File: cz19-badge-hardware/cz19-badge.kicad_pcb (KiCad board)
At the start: 4 copper layers, 169 x 56.5 mm, 445 parts, among them J1 USB_B_Micro, Q1 AO3400 (A09T), Q2 AO3400 (A09T), Q3 AO3400 (A09T), Q4 AO3400 (A09T), Q5 AO3400 (A09T), Q6 AO3400 (A09T), Q7 AO3400 (A09T), Q8 AO3400 (A09T), Q9 AO3400 (A09T), SW1 SW_Push, SW2 SW_Push, SW3 SW_Push, SW4 SW_Push, SW5 SW_Push, SW6 SW_Push, U1 CH340C, U2 AMS1117, U3 ESP32-WROOM-32D, U4 TP4056

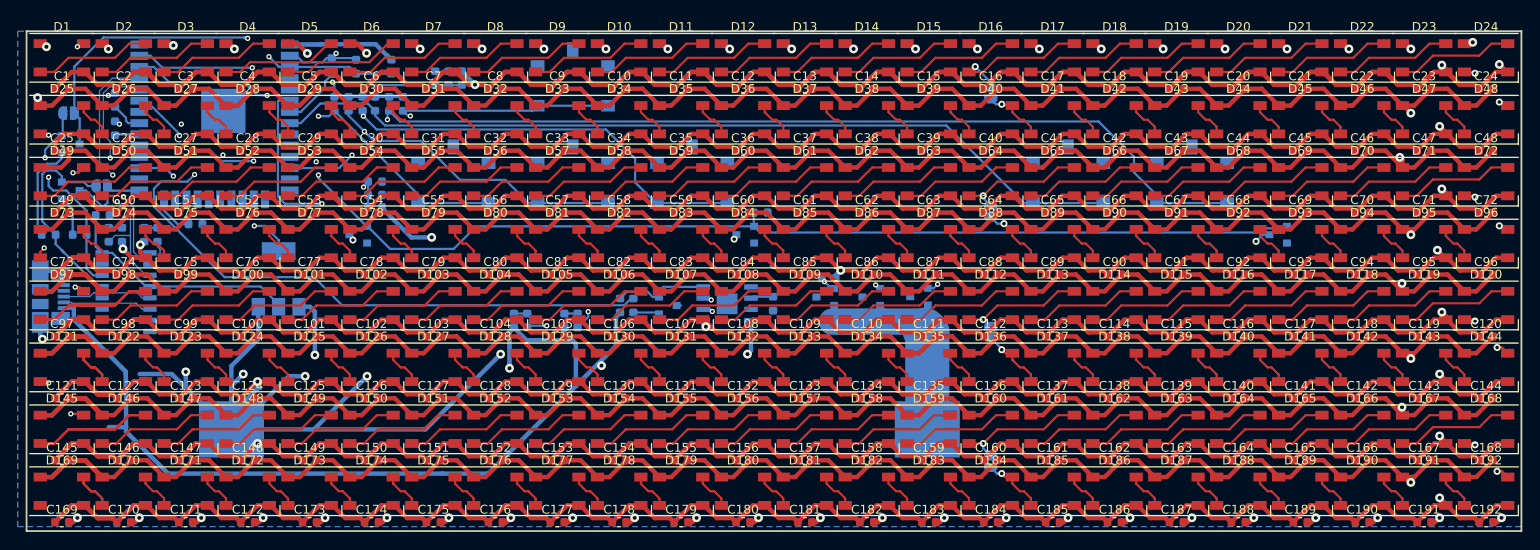
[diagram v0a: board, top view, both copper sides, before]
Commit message: Added experimental touch pad to center
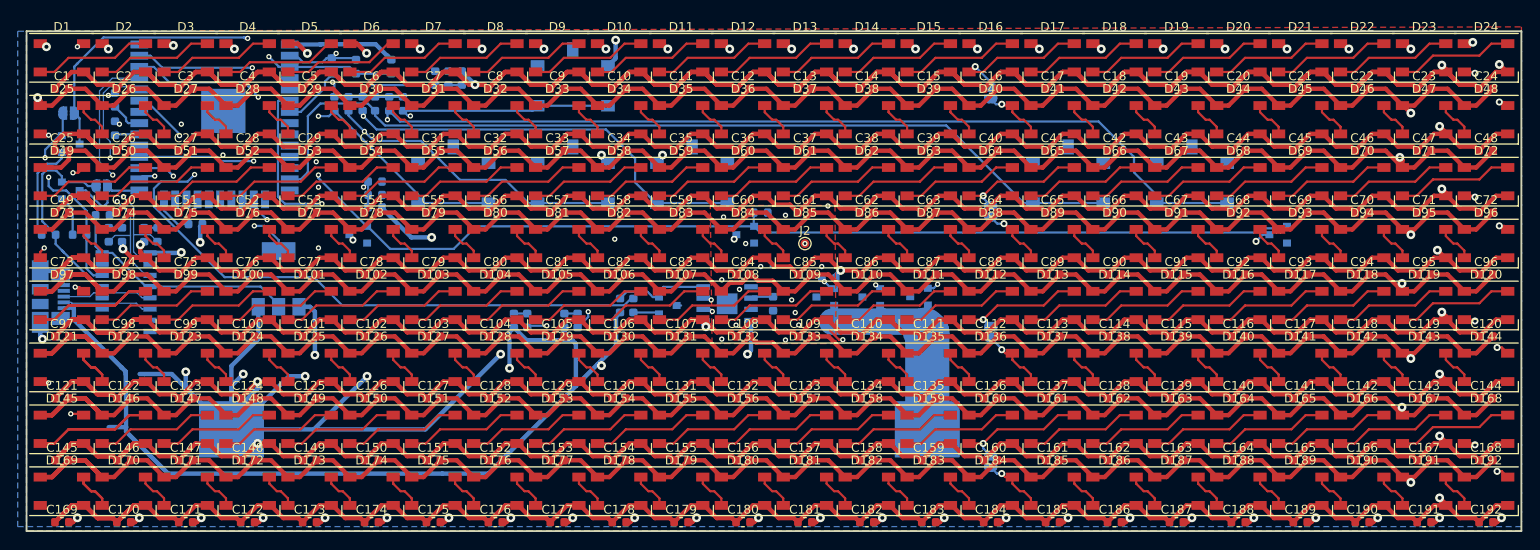
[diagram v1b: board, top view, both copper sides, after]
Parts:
- added J2: Conn_01x01, TestPoint:TestPoint_Pad_D1.0mm, F.Cu at (108.0, 46.0)
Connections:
- U1 pad 1: (no net) -> GND
- U3 pad 12: BTN_A -> (no net)
- U3 pad 13: (no net) -> BTN_B
- U3 pad 16: (no net) -> BTN_A
- U3 pad 26: (no net) -> TOUCH1
- U3 pad 8: BTN_B -> (no net)
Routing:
- net TOUCH1: track 0.00 -> 140.2 mm, vias 0 -> 19
- net GND: track 57.0 -> 92.1 mm, vias 2 -> 7
- net BTN_A: track 115.0 -> 122.9 mm, vias 2 -> 3
- net BTN_B: track 97.9 -> 104.2 mm
- added copper zone on F.Cu, net LED_GND
- added copper zone on F.Cu, net TOUCH1

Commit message: Fixed DRC warning
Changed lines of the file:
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@@
     (thickness 1.6)
     (drawings 8)
-    (tracks 3638)
+    (tracks 3639)
     (zones 0)
     (modules 446)
@@
   (segment (start 44.6 27.759998) (end 36.124998 27.759998) (width 0.25) (layer GND.Cu) (net 228))
   (segment (start 32.75 26.035) (end 34.4 26.035) (width 0.25) (layer GND.Cu) (net 228))
-  (via (at 46.20107 29.448029) (size 0.6) (drill 0.3) (layers F.Cu GND.Cu) (net 228))
-  (segment (start 45.840002 29) (end 45.840002 29.086961) (width 0.25) (layer GND.Cu) (net 228))
-  (segment (start 45.840002 29.086961) (end 46.20107 29.448029) (width 0.25) (layer GND.Cu) (net 228))
   (segment (start 44.6 27.759998) (end 45.840002 29) (width 0.25) (layer GND.Cu) (net 228))
-  (segment (start 51.3 29.9) (end 53 31.6) (width 0.25) (layer LGND.Cu) (net 228))
-  (segment (start 50.848029 29.448029) (end 51.3 29.9) (width 0.25) (layer LGND.Cu) (net 228))
-  (segment (start 46.20107 29.448029) (end 50.848029 29.448029) (width 0.25) (layer LGND.Cu) (net 228))
+  (via (at 46.2 29.8) (size 0.6) (drill 0.3) (layers F.Cu GND.Cu) (net 228))
+  (segment (start 53 31.6) (end 51.2 29.8) (width 0.25) (layer LGND.Cu) (net 228))
+  (segment (start 51.2 29.8) (end 46.624264 29.8) (width 0.25) (layer LGND.Cu) (net 228))
+  (segment (start 46.624264 29.8) (end 46.2 29.8) (width 0.25) (layer LGND.Cu) (net 228))
+  (segment (start 45.840002 29.015738) (end 45.840002 29) (width 0.25) (layer GND.Cu) (net 228))
+  (segment (start 46.2 29.375736) (end 45.840002 29.015738) (width 0.25) (layer GND.Cu) (net 228))
+  (segment (start 46.2 29.8) (end 46.2 29.375736) (width 0.25) (layer GND.Cu) (net 228))
   (segment (start 91.145 41.42) (end 91.27 41.42) (width 0.25) (layer GND.Cu) (net 229))
   (segment (start 88.8 39.075) (end 91.145 41.42) (width 0.25) (layer GND.Cu) (net 229))
@@
     (connect_pads (clearance 0.508))
     (min_thickness 0.254)
-    (fill yes (arc_segments 16) (thermal_gap 0.508) (thermal_bridge_width 0.508))
+    (fill yes (arc_segments 16) (thermal_gap 0.508) (thermal_bridge_width 0.3))
     (polygon
       (pts

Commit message: Added testpoint hooks
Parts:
- added J3: Hook1, TestPoint:TestPoint_Keystone_5019_Minature, B.Cu at (27.2, 26.2)
- added J4: Hook2, TestPoint:TestPoint_Keystone_5019_Minature, B.Cu at (173.6, 26.2)
- added J5: Hook3, TestPoint:TestPoint_Keystone_5019_Minature, B.Cu at (143.3, 63.7)
- added J6: Hook4, TestPoint:TestPoint_Keystone_5019_Minature, B.Cu at (158.3, 63.7)
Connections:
- D169 pad 4: (no net) -> LEDS_OUT
- J1 pad 4: (no net) -> Net-(J1-Pad4)
- U1 pad 10: (no net) -> Net-(U1-Pad10)
- U1 pad 11: (no net) -> Net-(U1-Pad11)
- U1 pad 12: (no net) -> Net-(U1-Pad12)
- U1 pad 15: (no net) -> Net-(U1-Pad15)
- U1 pad 7: (no net) -> Net-(U1-Pad7)
- U1 pad 8: (no net) -> Net-(U1-Pad8)
- U1 pad 9: (no net) -> Net-(U1-Pad9)
- U3 pad 10: (no net) -> DAC1
- U3 pad 11: (no net) -> DAC2
- U3 pad 12: (no net) -> Net-(U3-Pad12)
- U3 pad 14: (no net) -> Net-(U3-Pad14)
- U3 pad 17: (no net) -> Net-(U3-Pad17)
- U3 pad 18: (no net) -> Net-(U3-Pad18)
- U3 pad 19: (no net) -> Net-(U3-Pad19)
- U3 pad 20: (no net) -> Net-(U3-Pad20)
- U3 pad 21: (no net) -> Net-(U3-Pad21)
- U3 pad 22: (no net) -> Net-(U3-Pad22)
- U3 pad 23: (no net) -> Net-(U3-Pad23)
- U3 pad 29: (no net) -> Net-(U3-Pad29)
- U3 pad 32: (no net) -> Net-(U3-Pad32)
- U3 pad 4: (no net) -> Net-(U3-Pad4)
- U3 pad 5: (no net) -> Net-(U3-Pad5)
- U3 pad 8: (no net) -> Net-(U3-Pad8)
- U3 pad 9: (no net) -> Net-(U3-Pad9)
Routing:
- net ESP_EN: track 48.7 -> 51.4 mm
- net LEDS_IN: track 8.66 -> 9.71 mm
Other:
- board text added: "CZ19 1337 badge proto v0.1 aka “Harry Potter”"
- board text added: "Spoke width: 0.508mm"
- board text added: "Spoke width: 0.8mm"
- board text added: "Spoke width: 1.2mm"

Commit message: Working on non-smart leds
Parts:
- removed the C1 at (24.0, 28.5)
- removed C10, C100, C101, C102, C103, C104, C105, C106, C107, C108, C109, C11, C110, C111, C112, C113, C114, C115, C116, C117, C118, C119, C12, C120, C121, C122, C123, C124, C125, C126, C127, C128, C129, C13, C130, C131, C132, C133, C134, C135, C136, C137, C138, C139, C14, C140, C141, C142, C143, C144, C145, C146, C147, C148, C149, C15, C150, C151, C152, C153, C154, C155, C156, C157, C158, C159, C16, C160, C161, C162, C163, C164, C165, C166, C167, C168, C169, C17, C170, C171, C172, C173, C174, C175, C176, C177, C178, C179, C18, C180, C181, C182, C183, C184, C185, C186, C187, C188, C189, C19, C190, C191, C192, C20, C21, C22, C23, C24, C25, C26, C27, C28, C29, C30, C31, C32, C33, C34, C35, C36, C37, C38, C39, C40, C41, C42, C43, C44, C45, C46, C47, C48, C49, C5, C50, C51, C52, C53, C54, C55, C56, C57, C58, C59, C6, C60, C61, C62, C63, C64, C65, C66, C67, C68, C69, C7, C70, C71, C72, C73, C74, C75, C76, C77, C78, C79, C8, C80, C81, C82, C83, C84, C85, C86, C87, C88, C89, C9, C90, C91, C92, C93, C94, C95, C96, C97, C98, C99: 100nF, Capacitor_SMD:C_0603_1608Metric
- removed the C2 at (31.0, 28.5)
- removed the C3 at (38.0, 28.5)
- removed the C4 at (45.0, 28.5)
- removed J2: Conn_01x01, TestPoint:TestPoint_Pad_D1.0mm
- removed J5: Hook3, TestPoint:TestPoint_Keystone_5019_Minature
- removed J6: Hook4, TestPoint:TestPoint_Keystone_5019_Minature
- removed JP1, JP2, JP3, JP4, JP5, JP6: SolderJumper_2_Open, Jumper:SolderJumper-2_P1.3mm_Open_RoundedPad1.0x1.5mm
- removed the Q1 at (57.5, 45.0)
- removed the Q3 at (101.2, 45.0)
- removed the Q5 at (161.5, 45.0)
- removed the R8 at (30.0, 33.0)
- removed the R9 at (30.0, 29.8)
- added D193: LED_RGBA, LED_SMD:LED_Cree-PLCC4_3.2x2.8mm_CCW, F.Cu at (20.0, -120.0)
- added D194: LED_RGBA, LED_SMD:LED_Cree-PLCC4_3.2x2.8mm_CCW, F.Cu at (25.0, -120.0)
- added D195: LED_RGBA, LED_SMD:LED_Cree-PLCC4_3.2x2.8mm_CCW, F.Cu at (30.0, -120.0)
- added D196: LED_RGBA, LED_SMD:LED_Cree-PLCC4_3.2x2.8mm_CCW, F.Cu at (35.0, -120.0)
- added D197: LED_RGBA, LED_SMD:LED_Cree-PLCC4_3.2x2.8mm_CCW, F.Cu at (40.0, -120.0)
- added D198: LED_RGBA, LED_SMD:LED_Cree-PLCC4_3.2x2.8mm_CCW, F.Cu at (45.0, -120.0)
- added D199: LED_RGBA, LED_SMD:LED_Cree-PLCC4_3.2x2.8mm_CCW, F.Cu at (50.0, -120.0)
- added D200: LED_RGBA, LED_SMD:LED_Cree-PLCC4_3.2x2.8mm_CCW, F.Cu at (55.0, -120.0)
- added D201: LED_RGBA, LED_SMD:LED_Cree-PLCC4_3.2x2.8mm_CCW, F.Cu at (60.0, -120.0)
- added D202: LED_RGBA, LED_SMD:LED_Cree-PLCC4_3.2x2.8mm_CCW, F.Cu at (65.0, -120.0)
- added D203: LED_RGBA, LED_SMD:LED_Cree-PLCC4_3.2x2.8mm_CCW, F.Cu at (70.0, -120.0)
- added D204: LED_RGBA, LED_SMD:LED_Cree-PLCC4_3.2x2.8mm_CCW, F.Cu at (75.0, -120.0)
- added D205: LED_RGBA, LED_SMD:LED_Cree-PLCC4_3.2x2.8mm_CCW, F.Cu at (80.0, -120.0)
- added D206: LED_RGBA, LED_SMD:LED_Cree-PLCC4_3.2x2.8mm_CCW, F.Cu at (85.0, -120.0)
- added D207: LED_RGBA, LED_SMD:LED_Cree-PLCC4_3.2x2.8mm_CCW, F.Cu at (90.0, -120.0)
- added D208: LED_RGBA, LED_SMD:LED_Cree-PLCC4_3.2x2.8mm_CCW, F.Cu at (95.0, -120.0)
- added D209: LED_RGBA, LED_SMD:LED_Cree-PLCC4_3.2x2.8mm_CCW, F.Cu at (100.0, -120.0)
- added D210: LED_RGBA, LED_SMD:LED_Cree-PLCC4_3.2x2.8mm_CCW, F.Cu at (105.0, -120.0)
- added D211: LED_RGBA, LED_SMD:LED_Cree-PLCC4_3.2x2.8mm_CCW, F.Cu at (110.0, -120.0)
- added D212: LED_RGBA, LED_SMD:LED_Cree-PLCC4_3.2x2.8mm_CCW, F.Cu at (115.0, -120.0)
- added D213: LED_RGBA, LED_SMD:LED_Cree-PLCC4_3.2x2.8mm_CCW, F.Cu at (120.0, -120.0)
- added D214: LED_RGBA, LED_SMD:LED_Cree-PLCC4_3.2x2.8mm_CCW, F.Cu at (125.0, -120.0)
- added D215: LED_RGBA, LED_SMD:LED_Cree-PLCC4_3.2x2.8mm_CCW, F.Cu at (130.0, -120.0)
- added D216: LED_RGBA, LED_SMD:LED_Cree-PLCC4_3.2x2.8mm_CCW, F.Cu at (135.0, -120.0)
- added D217: LED_RGBA, LED_SMD:LED_Cree-PLCC4_3.2x2.8mm_CCW, F.Cu at (140.0, -120.0)
- added D218: LED_RGBA, LED_SMD:LED_Cree-PLCC4_3.2x2.8mm_CCW, F.Cu at (145.0, -120.0)
- added D219: LED_RGBA, LED_SMD:LED_Cree-PLCC4_3.2x2.8mm_CCW, F.Cu at (150.0, -120.0)
- added D220: LED_RGBA, LED_SMD:LED_Cree-PLCC4_3.2x2.8mm_CCW, F.Cu at (155.0, -120.0)
- added D221: LED_RGBA, LED_SMD:LED_Cree-PLCC4_3.2x2.8mm_CCW, F.Cu at (160.0, -120.0)
- added D222: LED_RGBA, LED_SMD:LED_Cree-PLCC4_3.2x2.8mm_CCW, F.Cu at (165.0, -120.0)
- added D223: LED_RGBA, LED_SMD:LED_Cree-PLCC4_3.2x2.8mm_CCW, F.Cu at (170.0, -120.0)
- added D224: LED_RGBA, LED_SMD:LED_Cree-PLCC4_3.2x2.8mm_CCW, F.Cu at (175.0, -120.0)
- added D225: LED_RGBA, LED_SMD:LED_Cree-PLCC4_3.2x2.8mm_CCW, F.Cu at (20.0, -115.0)
- added D226: LED_RGBA, LED_SMD:LED_Cree-PLCC4_3.2x2.8mm_CCW, F.Cu at (25.0, -115.0)
- added D227: LED_RGBA, LED_SMD:LED_Cree-PLCC4_3.2x2.8mm_CCW, F.Cu at (30.0, -115.0)
- added D228: LED_RGBA, LED_SMD:LED_Cree-PLCC4_3.2x2.8mm_CCW, F.Cu at (35.0, -115.0)
- added D229: LED_RGBA, LED_SMD:LED_Cree-PLCC4_3.2x2.8mm_CCW, F.Cu at (40.0, -115.0)
- added D230: LED_RGBA, LED_SMD:LED_Cree-PLCC4_3.2x2.8mm_CCW, F.Cu at (45.0, -115.0)
- added D231: LED_RGBA, LED_SMD:LED_Cree-PLCC4_3.2x2.8mm_CCW, F.Cu at (50.0, -115.0)
- added D232: LED_RGBA, LED_SMD:LED_Cree-PLCC4_3.2x2.8mm_CCW, F.Cu at (55.0, -115.0)
- added D233: LED_RGBA, LED_SMD:LED_Cree-PLCC4_3.2x2.8mm_CCW, F.Cu at (60.0, -115.0)
- added D234: LED_RGBA, LED_SMD:LED_Cree-PLCC4_3.2x2.8mm_CCW, F.Cu at (65.0, -115.0)
- added D235: LED_RGBA, LED_SMD:LED_Cree-PLCC4_3.2x2.8mm_CCW, F.Cu at (70.0, -115.0)
- added D236: LED_RGBA, LED_SMD:LED_Cree-PLCC4_3.2x2.8mm_CCW, F.Cu at (75.0, -115.0)
- added D237: LED_RGBA, LED_SMD:LED_Cree-PLCC4_3.2x2.8mm_CCW, F.Cu at (80.0, -115.0)
- added D238: LED_RGBA, LED_SMD:LED_Cree-PLCC4_3.2x2.8mm_CCW, F.Cu at (85.0, -115.0)
- added D239: LED_RGBA, LED_SMD:LED_Cree-PLCC4_3.2x2.8mm_CCW, F.Cu at (90.0, -115.0)
- added D240: LED_RGBA, LED_SMD:LED_Cree-PLCC4_3.2x2.8mm_CCW, F.Cu at (95.0, -115.0)
- added D241: LED_RGBA, LED_SMD:LED_Cree-PLCC4_3.2x2.8mm_CCW, F.Cu at (100.0, -115.0)
- added D242: LED_RGBA, LED_SMD:LED_Cree-PLCC4_3.2x2.8mm_CCW, F.Cu at (105.0, -115.0)
- added D243: LED_RGBA, LED_SMD:LED_Cree-PLCC4_3.2x2.8mm_CCW, F.Cu at (110.0, -115.0)
- added D244: LED_RGBA, LED_SMD:LED_Cree-PLCC4_3.2x2.8mm_CCW, F.Cu at (115.0, -115.0)
- added D245: LED_RGBA, LED_SMD:LED_Cree-PLCC4_3.2x2.8mm_CCW, F.Cu at (120.0, -115.0)
- added D246: LED_RGBA, LED_SMD:LED_Cree-PLCC4_3.2x2.8mm_CCW, F.Cu at (125.0, -115.0)
- added D247: LED_RGBA, LED_SMD:LED_Cree-PLCC4_3.2x2.8mm_CCW, F.Cu at (130.0, -115.0)
- added D248: LED_RGBA, LED_SMD:LED_Cree-PLCC4_3.2x2.8mm_CCW, F.Cu at (135.0, -115.0)
- added D249: LED_RGBA, LED_SMD:LED_Cree-PLCC4_3.2x2.8mm_CCW, F.Cu at (140.0, -115.0)
- added D250: LED_RGBA, LED_SMD:LED_Cree-PLCC4_3.2x2.8mm_CCW, F.Cu at (145.0, -115.0)
- added D251: LED_RGBA, LED_SMD:LED_Cree-PLCC4_3.2x2.8mm_CCW, F.Cu at (150.0, -115.0)
- added D252: LED_RGBA, LED_SMD:LED_Cree-PLCC4_3.2x2.8mm_CCW, F.Cu at (155.0, -115.0)
- added D253: LED_RGBA, LED_SMD:LED_Cree-PLCC4_3.2x2.8mm_CCW, F.Cu at (160.0, -115.0)
- added D254: LED_RGBA, LED_SMD:LED_Cree-PLCC4_3.2x2.8mm_CCW, F.Cu at (165.0, -115.0)
- added D255: LED_RGBA, LED_SMD:LED_Cree-PLCC4_3.2x2.8mm_CCW, F.Cu at (170.0, -115.0)
- added D256: LED_RGBA, LED_SMD:LED_Cree-PLCC4_3.2x2.8mm_CCW, F.Cu at (175.0, -115.0)
- added R1: R, Resistor_SMD:R_0603_1608Metric, F.Cu at (263.2, 108.0)
- added R20: 10k, Resistor_SMD:R_0603_1608Metric, F.Cu at (239.2, 116.3)
- added R21: 10k, Resistor_SMD:R_0603_1608Metric, F.Cu at (239.2, 114.8)
- added R23: 10k, Resistor_SMD:R_0603_1608Metric, F.Cu at (239.2, 113.3)
- added R3: R, Resistor_SMD:R_0603_1608Metric, F.Cu at (257.2, 108.0)
- added R4: R, Resistor_SMD:R_0603_1608Metric, F.Cu at (254.2, 108.0)
- added R5: R, Resistor_SMD:R_0603_1608Metric, F.Cu at (251.2, 108.0)
- added R6: R, Resistor_SMD:R_0603_1608Metric, F.Cu at (240.9, 80.4)
- added U1: SM16106, Package_SO:QSOP-24_3.9x8.7mm_P0.635mm, F.Cu at (243.1, 67.9)
- added U10: XC6206P332PR, Package_TO_SOT_SMD:SOT-89-3, F.Cu at (234.4, 115.1)
- added U11: ESP32-WROOM-32D, RF_Module:ESP32-WROOM-32, B.Cu at (30.6, -142.5)
- added U4: SM16106, Package_SO:QSOP-24_3.9x8.7mm_P0.635mm, F.Cu at (243.1, 58.6)
- added U5: SM16106, Package_SO:QSOP-24_3.9x8.7mm_P0.635mm, F.Cu at (235.6, 67.9)
- added U6: SM16106, Package_SO:QSOP-24_3.9x8.7mm_P0.635mm, F.Cu at (235.6, 58.6)
- added U7: TC7258E, Package_SO:SSOP-16_3.9x4.9mm_P0.635mm, F.Cu at (235.4, 84.6)
- D1, D10, D100, D101, D102, D103, D104, D105, D106, D107, D108, D109, D11, D110, D111, D112, D113, D114, D115, D116, D117, D118, D119, D12, D120, D121, D122, D123, D124, D125, D126, D127, D128, D129, D13, D130, D131, D132, D133, D134, D135, D136, D137, D138, D139, D14, D140, D141, D142, D143, D144, D145, D146, D147, D148, D149, D15, D150, D151, D152, D153, D154, D155, D156, D157, D158, D159, D16, D160, D161, D162, D163, D164, D165, D166, D167, D168, D169, D17, D170, D171, D172, D173, D174, D175, D176, D177, D178, D179, D18, D180, D181, D182, D183, D184, D185, D186, D187, D188, D189, D19, D190, D191, D192, D2, D20, D21, D22, D23, D24, D25, D26, D27, D28, D29, D3, D30, D31, D32, D33, D34, D35, D36, D37, D38, D39, D4, D40, D41, D42, D43, D44, D45, D46, D47, D48, D49, D5, D50, D51, D52, D53, D54, D55, D56, D57, D58, D59, D6, D60, D61, D62, D63, D64, D65, D66, D67, D68, D69, D7, D70, D71, D72, D73, D74, D75, D76, D77, D78, D79, D8, D80, D81, D82, D83, D84, D85, D86, D87, D88, D89, D9, D90, D91, D92, D93, D94, D95, D96, D97, D98, D99: value SK6812 -> LED_RGBA; footprint LED_SMD:LED_SK6812_PLCC4_5.0x5.0mm_P3.2mm -> LED_SMD:LED_Cree-PLCC4_3.2x2.8mm_CCW
- R2: value 10k -> R; moved to F.Cu
- U2: value AMS1117 -> SM16106; footprint Package_TO_SOT_SMD:SOT-223-3_TabPin2 -> Package_SO:QSOP-24_3.9x8.7mm_P0.635mm; moved to F.Cu
- U3: value ESP32-WROOM-32D -> SM16106; footprint RF_Module:ESP32-WROOM-32 -> Package_SO:QSOP-24_3.9x8.7mm_P0.635mm; moved to F.Cu
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- renumbered C193 to C1, C194 to C2, C195 to C3, C196 to C4, D193 to D257, D194 to D258, D195 to D259, D196 to D260, Q2 to Q1, Q4 to Q2, Q8 to Q3, Q6 to Q4, Q7 to Q5, Q9 to Q6, R11 to R10, R12 to R11, R13 to R12, R14 to R13, R15 to R14, R4 to R15, R5 to R16, R21 to R17, R6 to R18, R22 to R19, R7 to R22, R18 to R24, R16 to R25, R17 to R26, R19 to R27, R20 to R28, R23 to R29, R24 to R30, R25 to R31, R26 to R32, R1 to R7, R3 to R8, R10 to R9, U1 to U8, U4 to U9
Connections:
- D1 pad 1: VCC -> Net-(D1-Pad1)
- D1 pad 2: LEDS_IN -> Net-(D1-Pad2)
- D1 pad 3: LED_GND -> Net-(D1-Pad3)
- D10 pad 1: VCC -> Net-(D10-Pad1)
- D10 pad 3: LED_GND -> Net-(D10-Pad3)
- D10 pad 4: Net-(D10-Pad4) -> Net-(D1-Pad4)
- D100 pad 1: VCC -> Net-(D100-Pad1)
- D100 pad 3: LED_GND -> Net-(D100-Pad3)
- D101 pad 1: VCC -> Net-(D101-Pad1)
- D101 pad 2: Net-(D100-Pad4) -> Net-(D101-Pad2)
- D101 pad 3: LED_GND -> Net-(D101-Pad3)
- D101 pad 4: Net-(D101-Pad4) -> Net-(D100-Pad4)
- D102 pad 1: VCC -> Net-(D102-Pad1)
- D102 pad 2: Net-(D101-Pad4) -> Net-(D102-Pad2)
- D102 pad 3: LED_GND -> Net-(D102-Pad3)
- D102 pad 4: Net-(D102-Pad4) -> Net-(D100-Pad4)
- D103 pad 1: VCC -> Net-(D103-Pad1)
- D103 pad 2: Net-(D102-Pad4) -> Net-(D103-Pad2)
- D103 pad 3: LED_GND -> Net-(D103-Pad3)
- D103 pad 4: Net-(D103-Pad4) -> Net-(D100-Pad4)
- D104 pad 1: VCC -> Net-(D104-Pad1)
- D104 pad 2: Net-(D103-Pad4) -> Net-(D104-Pad2)
- D104 pad 3: LED_GND -> Net-(D104-Pad3)
- D104 pad 4: Net-(D104-Pad4) -> Net-(D100-Pad4)
- D105 pad 1: VCC -> Net-(D105-Pad1)
- D105 pad 2: Net-(D104-Pad4) -> Net-(D105-Pad2)
- D105 pad 3: LED_GND -> Net-(D105-Pad3)
- D105 pad 4: Net-(D105-Pad4) -> Net-(D100-Pad4)
- D106 pad 1: VCC -> Net-(D10-Pad1)
- D106 pad 2: Net-(D105-Pad4) -> Net-(D10-Pad2)
- D106 pad 3: LED_GND -> Net-(D10-Pad3)
- D106 pad 4: Net-(D106-Pad4) -> Net-(D100-Pad4)
- D107 pad 1: VCC -> Net-(D107-Pad1)
- D107 pad 2: Net-(D106-Pad4) -> Net-(D107-Pad2)
- D107 pad 3: LED_GND -> Net-(D107-Pad3)
- D107 pad 4: Net-(D107-Pad4) -> Net-(D100-Pad4)
- D108 pad 1: VCC -> Net-(D108-Pad1)
- D108 pad 2: Net-(D107-Pad4) -> Net-(D108-Pad2)
- D108 pad 3: LED_GND -> Net-(D108-Pad3)
- D108 pad 4: Net-(D108-Pad4) -> Net-(D100-Pad4)
- D109 pad 1: VCC -> Net-(D109-Pad1)
- D109 pad 2: Net-(D108-Pad4) -> Net-(D109-Pad2)
- D109 pad 3: LED_GND -> Net-(D109-Pad3)
- D109 pad 4: Net-(D109-Pad4) -> Net-(D100-Pad4)
- D11 pad 1: VCC -> Net-(D107-Pad1)
- D11 pad 2: Net-(D10-Pad4) -> Net-(D107-Pad2)
- D11 pad 3: LED_GND -> Net-(D107-Pad3)
- D11 pad 4: Net-(D11-Pad4) -> Net-(D1-Pad4)
- D110 pad 1: VCC -> Net-(D110-Pad1)
- D110 pad 2: Net-(D109-Pad4) -> Net-(D110-Pad2)
- D110 pad 3: LED_GND -> Net-(D110-Pad3)
- D110 pad 4: Net-(D110-Pad4) -> Net-(D100-Pad4)
- D111 pad 1: VCC -> Net-(D111-Pad1)
- D111 pad 2: Net-(D110-Pad4) -> Net-(D111-Pad2)
- D111 pad 3: LED_GND -> Net-(D111-Pad3)
- D111 pad 4: Net-(D111-Pad4) -> Net-(D100-Pad4)
- D112 pad 1: VCC -> Net-(D112-Pad1)
- D112 pad 2: Net-(D111-Pad4) -> Net-(D112-Pad2)
- D112 pad 3: LED_GND -> Net-(D112-Pad3)
- D112 pad 4: Net-(D112-Pad4) -> Net-(D100-Pad4)
- D113 pad 1: VCC -> Net-(D113-Pad1)
- D113 pad 2: Net-(D112-Pad4) -> Net-(D113-Pad2)
- D113 pad 3: LED_GND -> Net-(D113-Pad3)
- D113 pad 4: Net-(D113-Pad4) -> Net-(D100-Pad4)
- D114 pad 1: VCC -> Net-(D114-Pad1)
- D114 pad 2: Net-(D113-Pad4) -> Net-(D114-Pad2)
- D114 pad 3: LED_GND -> Net-(D114-Pad3)
- D114 pad 4: Net-(D114-Pad4) -> Net-(D100-Pad4)
- D115 pad 1: VCC -> Net-(D115-Pad1)
- D115 pad 2: Net-(D114-Pad4) -> Net-(D115-Pad2)
- D115 pad 3: LED_GND -> Net-(D115-Pad3)
- D115 pad 4: Net-(D115-Pad4) -> Net-(D100-Pad4)
- D116 pad 1: VCC -> Net-(D116-Pad1)
- D116 pad 2: Net-(D115-Pad4) -> Net-(D116-Pad2)
- D116 pad 3: LED_GND -> Net-(D116-Pad3)
- D116 pad 4: Net-(D116-Pad4) -> Net-(D100-Pad4)
- D117 pad 1: VCC -> Net-(D117-Pad1)
- D117 pad 2: Net-(D116-Pad4) -> Net-(D117-Pad2)
- D117 pad 3: LED_GND -> Net-(D117-Pad3)
- D117 pad 4: Net-(D117-Pad4) -> Net-(D100-Pad4)
- D118 pad 1: VCC -> Net-(D118-Pad1)
- D118 pad 2: Net-(D117-Pad4) -> Net-(D118-Pad2)
- D118 pad 3: LED_GND -> Net-(D118-Pad3)
- D118 pad 4: Net-(D118-Pad4) -> Net-(D100-Pad4)
- D119 pad 1: VCC -> Net-(D119-Pad1)
- D119 pad 2: Net-(D118-Pad4) -> Net-(D119-Pad2)
- D119 pad 3: LED_GND -> Net-(D119-Pad3)
- D119 pad 4: Net-(D119-Pad4) -> Net-(D100-Pad4)
- D12 pad 1: VCC -> Net-(D108-Pad1)
- D12 pad 2: Net-(D11-Pad4) -> Net-(D108-Pad2)
- D12 pad 3: LED_GND -> Net-(D108-Pad3)
- D12 pad 4: Net-(D12-Pad4) -> Net-(D1-Pad4)
- D120 pad 1: VCC -> Net-(D120-Pad1)
- D120 pad 2: Net-(D119-Pad4) -> Net-(D120-Pad2)
- D120 pad 3: LED_GND -> Net-(D120-Pad3)
- D120 pad 4: Net-(D120-Pad4) -> Net-(D100-Pad4)
- D121 pad 1: VCC -> Net-(D121-Pad1)
- D121 pad 3: LED_GND -> Net-(D121-Pad3)
- D121 pad 4: Net-(D121-Pad4) -> Net-(D100-Pad4)
- D122 pad 1: VCC -> Net-(D122-Pad1)
- D122 pad 3: LED_GND -> Net-(D122-Pad3)
- D122 pad 4: Net-(D121-Pad2) -> Net-(D100-Pad4)
- D123 pad 1: VCC -> Net-(D123-Pad1)
- D123 pad 3: LED_GND -> Net-(D123-Pad3)
- D123 pad 4: Net-(D122-Pad2) -> Net-(D100-Pad4)
- D124 pad 1: VCC -> Net-(D124-Pad1)
- D124 pad 3: LED_GND -> Net-(D124-Pad3)
- D124 pad 4: Net-(D123-Pad2) -> Net-(D100-Pad4)
- D125 pad 1: VCC -> Net-(D125-Pad1)
- D125 pad 3: LED_GND -> Net-(D125-Pad3)
- D125 pad 4: Net-(D124-Pad2) -> Net-(D100-Pad4)
- D126 pad 1: VCC -> Net-(D126-Pad1)
- D126 pad 3: LED_GND -> Net-(D126-Pad3)
- D126 pad 4: Net-(D125-Pad2) -> Net-(D100-Pad4)
- D127 pad 1: VCC -> Net-(D127-Pad1)
- D127 pad 3: LED_GND -> Net-(D127-Pad3)
- D127 pad 4: Net-(D126-Pad2) -> Net-(D100-Pad4)
- D128 pad 1: VCC -> Net-(D128-Pad1)
- D128 pad 3: LED_GND -> Net-(D128-Pad3)
- D128 pad 4: Net-(D127-Pad2) -> Net-(D100-Pad4)
- D129 pad 1: VCC -> Net-(D1-Pad1)
- D129 pad 2: Net-(D129-Pad2) -> Net-(D1-Pad2)
- D129 pad 3: LED_GND -> Net-(D1-Pad3)
- D129 pad 4: Net-(D128-Pad2) -> Net-(D129-Pad4)
- D13 pad 1: VCC -> Net-(D109-Pad1)
- D13 pad 2: Net-(D12-Pad4) -> Net-(D109-Pad2)
- D13 pad 3: LED_GND -> Net-(D109-Pad3)
- D13 pad 4: Net-(D13-Pad4) -> Net-(D1-Pad4)
- D130 pad 1: VCC -> Net-(D130-Pad1)
- D130 pad 3: LED_GND -> Net-(D130-Pad3)
- D130 pad 4: Net-(D129-Pad2) -> Net-(D129-Pad4)
- D131 pad 1: VCC -> Net-(D131-Pad1)
- D131 pad 3: LED_GND -> Net-(D131-Pad3)
- D131 pad 4: Net-(D130-Pad2) -> Net-(D129-Pad4)
- D132 pad 1: VCC -> Net-(D100-Pad1)
- D132 pad 2: Net-(D132-Pad2) -> Net-(D100-Pad2)
- D132 pad 3: LED_GND -> Net-(D100-Pad3)
- D132 pad 4: Net-(D131-Pad2) -> Net-(D129-Pad4)
- D133 pad 1: VCC -> Net-(D101-Pad1)
- D133 pad 2: Net-(D133-Pad2) -> Net-(D101-Pad2)
- D133 pad 3: LED_GND -> Net-(D101-Pad3)
- D133 pad 4: Net-(D132-Pad2) -> Net-(D129-Pad4)
- D134 pad 1: VCC -> Net-(D102-Pad1)
- D134 pad 2: Net-(D134-Pad2) -> Net-(D102-Pad2)
- D134 pad 3: LED_GND -> Net-(D102-Pad3)
- D134 pad 4: Net-(D133-Pad2) -> Net-(D129-Pad4)
- D135 pad 1: VCC -> Net-(D103-Pad1)
- D135 pad 2: Net-(D135-Pad2) -> Net-(D103-Pad2)
- D135 pad 3: LED_GND -> Net-(D103-Pad3)
- D135 pad 4: Net-(D134-Pad2) -> Net-(D129-Pad4)
- D136 pad 1: VCC -> Net-(D104-Pad1)
- D136 pad 2: Net-(D136-Pad2) -> Net-(D104-Pad2)
- D136 pad 3: LED_GND -> Net-(D104-Pad3)
- D136 pad 4: Net-(D135-Pad2) -> Net-(D129-Pad4)
- D137 pad 1: VCC -> Net-(D105-Pad1)
- D137 pad 2: Net-(D137-Pad2) -> Net-(D105-Pad2)
- D137 pad 3: LED_GND -> Net-(D105-Pad3)
- D137 pad 4: Net-(D136-Pad2) -> Net-(D129-Pad4)
- D138 pad 1: VCC -> Net-(D10-Pad1)
- D138 pad 2: Net-(D138-Pad2) -> Net-(D10-Pad2)
- D138 pad 3: LED_GND -> Net-(D10-Pad3)
- D138 pad 4: Net-(D137-Pad2) -> Net-(D129-Pad4)
- D139 pad 1: VCC -> Net-(D107-Pad1)
- D139 pad 2: Net-(D139-Pad2) -> Net-(D107-Pad2)
- D139 pad 3: LED_GND -> Net-(D107-Pad3)
- D139 pad 4: Net-(D138-Pad2) -> Net-(D129-Pad4)
- D14 pad 1: VCC -> Net-(D110-Pad1)
- D14 pad 2: Net-(D13-Pad4) -> Net-(D110-Pad2)
- D14 pad 3: LED_GND -> Net-(D110-Pad3)
- D14 pad 4: Net-(D14-Pad4) -> Net-(D1-Pad4)
- D140 pad 1: VCC -> Net-(D108-Pad1)
- D140 pad 2: Net-(D140-Pad2) -> Net-(D108-Pad2)
- D140 pad 3: LED_GND -> Net-(D108-Pad3)
- D140 pad 4: Net-(D139-Pad2) -> Net-(D129-Pad4)
- D141 pad 1: VCC -> Net-(D109-Pad1)
- D141 pad 2: Net-(D141-Pad2) -> Net-(D109-Pad2)
- D141 pad 3: LED_GND -> Net-(D109-Pad3)
- D141 pad 4: Net-(D140-Pad2) -> Net-(D129-Pad4)
- D142 pad 1: VCC -> Net-(D110-Pad1)
- D142 pad 2: Net-(D142-Pad2) -> Net-(D110-Pad2)
- D142 pad 3: LED_GND -> Net-(D110-Pad3)
- D142 pad 4: Net-(D141-Pad2) -> Net-(D129-Pad4)
- D143 pad 1: VCC -> Net-(D111-Pad1)
- D143 pad 2: Net-(D143-Pad2) -> Net-(D111-Pad2)
- D143 pad 3: LED_GND -> Net-(D111-Pad3)
- D143 pad 4: Net-(D142-Pad2) -> Net-(D129-Pad4)
- D144 pad 1: VCC -> Net-(D112-Pad1)
- D144 pad 2: Net-(D120-Pad4) -> Net-(D112-Pad2)
- D144 pad 3: LED_GND -> Net-(D112-Pad3)
- D144 pad 4: Net-(D143-Pad2) -> Net-(D129-Pad4)
- D145 pad 1: VCC -> Net-(D113-Pad1)
- D145 pad 2: Net-(D121-Pad4) -> Net-(D113-Pad2)
- D145 pad 3: LED_GND -> Net-(D113-Pad3)
- D145 pad 4: Net-(D145-Pad4) -> Net-(D129-Pad4)
- D146 pad 1: VCC -> Net-(D114-Pad1)
- D146 pad 2: Net-(D145-Pad4) -> Net-(D114-Pad2)
- D146 pad 3: LED_GND -> Net-(D114-Pad3)
- D146 pad 4: Net-(D146-Pad4) -> Net-(D129-Pad4)
- D147 pad 1: VCC -> Net-(D115-Pad1)
- D147 pad 2: Net-(D146-Pad4) -> Net-(D115-Pad2)
- D147 pad 3: LED_GND -> Net-(D115-Pad3)
- D147 pad 4: Net-(D147-Pad4) -> Net-(D129-Pad4)
- D148 pad 1: VCC -> Net-(D116-Pad1)
- D148 pad 2: Net-(D147-Pad4) -> Net-(D116-Pad2)
- D148 pad 3: LED_GND -> Net-(D116-Pad3)
- D148 pad 4: Net-(D148-Pad4) -> Net-(D129-Pad4)
- D149 pad 1: VCC -> Net-(D117-Pad1)
- D149 pad 2: Net-(D148-Pad4) -> Net-(D117-Pad2)
- D149 pad 3: LED_GND -> Net-(D117-Pad3)
- D149 pad 4: Net-(D149-Pad4) -> Net-(D129-Pad4)
- D15 pad 1: VCC -> Net-(D111-Pad1)
- D15 pad 2: Net-(D14-Pad4) -> Net-(D111-Pad2)
- D15 pad 3: LED_GND -> Net-(D111-Pad3)
- D15 pad 4: Net-(D15-Pad4) -> Net-(D1-Pad4)
- D150 pad 1: VCC -> Net-(D118-Pad1)
- D150 pad 2: Net-(D149-Pad4) -> Net-(D118-Pad2)
- D150 pad 3: LED_GND -> Net-(D118-Pad3)
- D150 pad 4: Net-(D150-Pad4) -> Net-(D129-Pad4)
- D151 pad 1: VCC -> Net-(D119-Pad1)
- D151 pad 2: Net-(D150-Pad4) -> Net-(D119-Pad2)
- D151 pad 3: LED_GND -> Net-(D119-Pad3)
- D151 pad 4: Net-(D151-Pad4) -> Net-(D129-Pad4)
- D152 pad 1: VCC -> Net-(D120-Pad1)
- D152 pad 2: Net-(D151-Pad4) -> Net-(D120-Pad2)
- D152 pad 3: LED_GND -> Net-(D120-Pad3)
- D152 pad 4: Net-(D152-Pad4) -> Net-(D129-Pad4)
- D153 pad 1: VCC -> Net-(D121-Pad1)
- D153 pad 2: Net-(D152-Pad4) -> Net-(D121-Pad2)
- D153 pad 3: LED_GND -> Net-(D121-Pad3)
- D153 pad 4: Net-(D153-Pad4) -> Net-(D129-Pad4)
- D154 pad 1: VCC -> Net-(D122-Pad1)
- D154 pad 2: Net-(D153-Pad4) -> Net-(D122-Pad2)
- D154 pad 3: LED_GND -> Net-(D122-Pad3)
- D154 pad 4: Net-(D154-Pad4) -> Net-(D129-Pad4)
- D155 pad 1: VCC -> Net-(D123-Pad1)
- D155 pad 2: Net-(D154-Pad4) -> Net-(D123-Pad2)
- D155 pad 3: LED_GND -> Net-(D123-Pad3)
- D155 pad 4: Net-(D155-Pad4) -> Net-(D129-Pad4)
- D156 pad 1: VCC -> Net-(D124-Pad1)
- D156 pad 2: Net-(D155-Pad4) -> Net-(D124-Pad2)
- D156 pad 3: LED_GND -> Net-(D124-Pad3)
- D156 pad 4: Net-(D156-Pad4) -> Net-(D129-Pad4)
- D157 pad 1: VCC -> Net-(D125-Pad1)
- D157 pad 2: Net-(D156-Pad4) -> Net-(D125-Pad2)
- D157 pad 3: LED_GND -> Net-(D125-Pad3)
- D157 pad 4: Net-(D157-Pad4) -> Net-(D129-Pad4)
- D158 pad 1: VCC -> Net-(D126-Pad1)
- D158 pad 2: Net-(D157-Pad4) -> Net-(D126-Pad2)
- D158 pad 3: LED_GND -> Net-(D126-Pad3)
- D158 pad 4: Net-(D158-Pad4) -> Net-(D129-Pad4)
- D159 pad 1: VCC -> Net-(D127-Pad1)
- D159 pad 2: Net-(D158-Pad4) -> Net-(D127-Pad2)
- D159 pad 3: LED_GND -> Net-(D127-Pad3)
- D159 pad 4: Net-(D159-Pad4) -> Net-(D129-Pad4)
- D16 pad 1: VCC -> Net-(D112-Pad1)
- D16 pad 2: Net-(D15-Pad4) -> Net-(D112-Pad2)
- D16 pad 3: LED_GND -> Net-(D112-Pad3)
- D16 pad 4: Net-(D16-Pad4) -> Net-(D1-Pad4)
- D160 pad 1: VCC -> Net-(D128-Pad1)
- D160 pad 2: Net-(D159-Pad4) -> Net-(D128-Pad2)
- D160 pad 3: LED_GND -> Net-(D128-Pad3)
- D160 pad 4: Net-(D160-Pad4) -> Net-(D129-Pad4)
- D161 pad 1: VCC -> Net-(D1-Pad1)
- D161 pad 2: Net-(D160-Pad4) -> Net-(D1-Pad2)
- D161 pad 3: LED_GND -> Net-(D1-Pad3)
- D162 pad 1: VCC -> Net-(D130-Pad1)
- D162 pad 2: Net-(D161-Pad4) -> Net-(D130-Pad2)
- D162 pad 3: LED_GND -> Net-(D130-Pad3)
- D162 pad 4: Net-(D162-Pad4) -> Net-(D161-Pad4)
- D163 pad 1: VCC -> Net-(D131-Pad1)
- D163 pad 2: Net-(D162-Pad4) -> Net-(D131-Pad2)
- D163 pad 3: LED_GND -> Net-(D131-Pad3)
- D163 pad 4: Net-(D163-Pad4) -> Net-(D161-Pad4)
- D164 pad 1: VCC -> Net-(D100-Pad1)
- D164 pad 2: Net-(D163-Pad4) -> Net-(D100-Pad2)
- D164 pad 3: LED_GND -> Net-(D100-Pad3)
- D164 pad 4: Net-(D164-Pad4) -> Net-(D161-Pad4)
- D165 pad 1: VCC -> Net-(D101-Pad1)
- D165 pad 2: Net-(D164-Pad4) -> Net-(D101-Pad2)
- D165 pad 3: LED_GND -> Net-(D101-Pad3)
- D165 pad 4: Net-(D165-Pad4) -> Net-(D161-Pad4)
- D166 pad 1: VCC -> Net-(D102-Pad1)
- D166 pad 2: Net-(D165-Pad4) -> Net-(D102-Pad2)
- D166 pad 3: LED_GND -> Net-(D102-Pad3)
- D166 pad 4: Net-(D166-Pad4) -> Net-(D161-Pad4)
- D167 pad 1: VCC -> Net-(D103-Pad1)
- D167 pad 2: Net-(D166-Pad4) -> Net-(D103-Pad2)
- D167 pad 3: LED_GND -> Net-(D103-Pad3)
- D167 pad 4: Net-(D167-Pad4) -> Net-(D161-Pad4)
- D168 pad 1: VCC -> Net-(D104-Pad1)
- D168 pad 2: Net-(D167-Pad4) -> Net-(D104-Pad2)
- D168 pad 3: LED_GND -> Net-(D104-Pad3)
- D168 pad 4: Net-(D168-Pad4) -> Net-(D161-Pad4)
- D169 pad 1: VCC -> Net-(D105-Pad1)
- D169 pad 2: Net-(D169-Pad2) -> Net-(D105-Pad2)
- D169 pad 3: LED_GND -> Net-(D105-Pad3)
- D169 pad 4: LEDS_OUT -> Net-(D161-Pad4)
- D17 pad 1: VCC -> Net-(D113-Pad1)
- D17 pad 2: Net-(D16-Pad4) -> Net-(D113-Pad2)
- D17 pad 3: LED_GND -> Net-(D113-Pad3)
- D17 pad 4: Net-(D17-Pad4) -> Net-(D1-Pad4)
- D170 pad 1: VCC -> Net-(D10-Pad1)
- D170 pad 2: Net-(D170-Pad2) -> Net-(D10-Pad2)
- D170 pad 3: LED_GND -> Net-(D10-Pad3)
- D170 pad 4: Net-(D169-Pad2) -> Net-(D161-Pad4)
- D171 pad 1: VCC -> Net-(D107-Pad1)
- D171 pad 2: Net-(D171-Pad2) -> Net-(D107-Pad2)
- D171 pad 3: LED_GND -> Net-(D107-Pad3)
- D171 pad 4: Net-(D170-Pad2) -> Net-(D161-Pad4)
- D172 pad 1: VCC -> Net-(D108-Pad1)
- D172 pad 2: Net-(D172-Pad2) -> Net-(D108-Pad2)
- D172 pad 3: LED_GND -> Net-(D108-Pad3)
- D172 pad 4: Net-(D171-Pad2) -> Net-(D161-Pad4)
- D173 pad 1: VCC -> Net-(D109-Pad1)
- D173 pad 2: Net-(D173-Pad2) -> Net-(D109-Pad2)
- D173 pad 3: LED_GND -> Net-(D109-Pad3)
- D173 pad 4: Net-(D172-Pad2) -> Net-(D161-Pad4)
- D174 pad 1: VCC -> Net-(D110-Pad1)
- D174 pad 2: Net-(D174-Pad2) -> Net-(D110-Pad2)
- D174 pad 3: LED_GND -> Net-(D110-Pad3)
- D174 pad 4: Net-(D173-Pad2) -> Net-(D161-Pad4)
- D175 pad 1: VCC -> Net-(D111-Pad1)
- D175 pad 2: Net-(D175-Pad2) -> Net-(D111-Pad2)
- D175 pad 3: LED_GND -> Net-(D111-Pad3)
- D175 pad 4: Net-(D174-Pad2) -> Net-(D161-Pad4)
- D176 pad 1: VCC -> Net-(D112-Pad1)
- D176 pad 2: Net-(D176-Pad2) -> Net-(D112-Pad2)
- D176 pad 3: LED_GND -> Net-(D112-Pad3)
- D176 pad 4: Net-(D175-Pad2) -> Net-(D161-Pad4)
- D177 pad 1: VCC -> Net-(D113-Pad1)
- D177 pad 2: Net-(D177-Pad2) -> Net-(D113-Pad2)
- D177 pad 3: LED_GND -> Net-(D113-Pad3)
- D177 pad 4: Net-(D176-Pad2) -> Net-(D161-Pad4)
- D178 pad 1: VCC -> Net-(D114-Pad1)
- D178 pad 2: Net-(D178-Pad2) -> Net-(D114-Pad2)
- D178 pad 3: LED_GND -> Net-(D114-Pad3)
- D178 pad 4: Net-(D177-Pad2) -> Net-(D161-Pad4)
- D179 pad 1: VCC -> Net-(D115-Pad1)
- D179 pad 2: Net-(D179-Pad2) -> Net-(D115-Pad2)
- D179 pad 3: LED_GND -> Net-(D115-Pad3)
- D179 pad 4: Net-(D178-Pad2) -> Net-(D161-Pad4)
- D18 pad 1: VCC -> Net-(D114-Pad1)
- D18 pad 2: Net-(D17-Pad4) -> Net-(D114-Pad2)
- D18 pad 3: LED_GND -> Net-(D114-Pad3)
- D18 pad 4: Net-(D18-Pad4) -> Net-(D1-Pad4)
- D180 pad 1: VCC -> Net-(D116-Pad1)
- D180 pad 2: Net-(D180-Pad2) -> Net-(D116-Pad2)
- D180 pad 3: LED_GND -> Net-(D116-Pad3)
- D180 pad 4: Net-(D179-Pad2) -> Net-(D161-Pad4)
- D181 pad 1: VCC -> Net-(D117-Pad1)
- D181 pad 2: Net-(D181-Pad2) -> Net-(D117-Pad2)
- D181 pad 3: LED_GND -> Net-(D117-Pad3)
- D181 pad 4: Net-(D180-Pad2) -> Net-(D161-Pad4)
- D182 pad 1: VCC -> Net-(D118-Pad1)
- D182 pad 2: Net-(D182-Pad2) -> Net-(D118-Pad2)
- D182 pad 3: LED_GND -> Net-(D118-Pad3)
- D182 pad 4: Net-(D181-Pad2) -> Net-(D161-Pad4)
- D183 pad 1: VCC -> Net-(D119-Pad1)
- D183 pad 2: Net-(D183-Pad2) -> Net-(D119-Pad2)
- D183 pad 3: LED_GND -> Net-(D119-Pad3)
- D183 pad 4: Net-(D182-Pad2) -> Net-(D161-Pad4)
- D184 pad 1: VCC -> Net-(D120-Pad1)
- D184 pad 2: Net-(D184-Pad2) -> Net-(D120-Pad2)
- D184 pad 3: LED_GND -> Net-(D120-Pad3)
- D184 pad 4: Net-(D183-Pad2) -> Net-(D161-Pad4)
- D185 pad 1: VCC -> Net-(D121-Pad1)
- D185 pad 2: Net-(D185-Pad2) -> Net-(D121-Pad2)
- D185 pad 3: LED_GND -> Net-(D121-Pad3)
- D185 pad 4: Net-(D184-Pad2) -> Net-(D161-Pad4)
- D186 pad 1: VCC -> Net-(D122-Pad1)
- D186 pad 2: Net-(D186-Pad2) -> Net-(D122-Pad2)
- D186 pad 3: LED_GND -> Net-(D122-Pad3)
- D186 pad 4: Net-(D185-Pad2) -> Net-(D161-Pad4)
- D187 pad 1: VCC -> Net-(D123-Pad1)
- D187 pad 2: Net-(D187-Pad2) -> Net-(D123-Pad2)
- D187 pad 3: LED_GND -> Net-(D123-Pad3)
- D187 pad 4: Net-(D186-Pad2) -> Net-(D161-Pad4)
- D188 pad 1: VCC -> Net-(D124-Pad1)
- D188 pad 2: Net-(D188-Pad2) -> Net-(D124-Pad2)
- D188 pad 3: LED_GND -> Net-(D124-Pad3)
- D188 pad 4: Net-(D187-Pad2) -> Net-(D161-Pad4)
- D189 pad 1: VCC -> Net-(D125-Pad1)
- D189 pad 2: Net-(D189-Pad2) -> Net-(D125-Pad2)
- D189 pad 3: LED_GND -> Net-(D125-Pad3)
- D189 pad 4: Net-(D188-Pad2) -> Net-(D161-Pad4)
- D19 pad 1: VCC -> Net-(D115-Pad1)
- D19 pad 2: Net-(D18-Pad4) -> Net-(D115-Pad2)
- D19 pad 3: LED_GND -> Net-(D115-Pad3)
- D19 pad 4: Net-(D19-Pad4) -> Net-(D1-Pad4)
- D190 pad 1: VCC -> Net-(D126-Pad1)
- D190 pad 2: Net-(D190-Pad2) -> Net-(D126-Pad2)
- D190 pad 3: LED_GND -> Net-(D126-Pad3)
- D190 pad 4: Net-(D189-Pad2) -> Net-(D161-Pad4)
- D191 pad 1: VCC -> Net-(D127-Pad1)
- D191 pad 2: Net-(D191-Pad2) -> Net-(D127-Pad2)
- D191 pad 3: LED_GND -> Net-(D127-Pad3)
- D191 pad 4: Net-(D190-Pad2) -> Net-(D161-Pad4)
- D192 pad 1: VCC -> Net-(D128-Pad1)
- D192 pad 2: Net-(D168-Pad4) -> Net-(D128-Pad2)
- D192 pad 3: LED_GND -> Net-(D128-Pad3)
- D192 pad 4: Net-(D191-Pad2) -> Net-(D161-Pad4)
- D2 pad 1: VCC -> Net-(D130-Pad1)
- D2 pad 2: Net-(D1-Pad4) -> Net-(D130-Pad2)
- D2 pad 3: LED_GND -> Net-(D130-Pad3)
- D2 pad 4: Net-(D2-Pad4) -> Net-(D1-Pad4)
- D20 pad 1: VCC -> Net-(D116-Pad1)
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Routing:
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- removed copper zone on B.Cu, net GND
- removed copper zone on F.Cu, net LED_GND
- removed copper zone on LGND.Cu, net LED_GND
- removed copper zone on F.Cu, net TOUCH1
- removed copper zone on VCC.Cu, net VCC

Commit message: Having a small panic attack due to super small real estate at 5mm pixel pitch
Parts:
- R1, R2, R20, R21, R23, R3, R4, R5, R6, U1, U10, U2, U3, U4, U5, U6, U7: moved to B.Cu
- moved U10 306.2 mm to (62.1, -138.0)
- moved U9 296.3 mm to (121.2, -138.3)
- moved SW2 293.5 mm to (83.7, -144.8)
- moved SW4 293.5 mm to (97.2, -144.8)
- moved J1 285.1 mm to (19.6, -120.6)
- moved R18 284.5 mm to (41.7, -130.1), turned to 0 degrees
- moved U8 281.7 mm to (31.4, -118.7), turned to 270 degrees
- moved SW5 279.3 mm to (173.7, -135.4), turned to 270 degrees
- moved SW1 272.9 mm to (168.2, -147.6)
- moved SW3 272.0 mm to (164.7, -135.4), turned to 270 degrees
- moved SW6 266.8 mm to (168.1, -124.5)
- moved U7 244.1 mm to (136.1, -138.4)
- moved U3 232.0 mm to (145.6, -136.7)
- moved U2 213.3 mm to (145.7, -127.2)
- moved U6 211.0 mm to (155.8, -136.7)
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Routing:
- net C: track 0.00 -> 45.9 mm
- net SCL: track 0.00 -> 43.9 mm
- net B: track 0.00 -> 39.1 mm
- net A: track 0.00 -> 37.1 mm
- net SDA: track 0.00 -> 34.2 mm
- net ESP_FLASH: track 0.00 -> 30.3 mm
- net G0: track 0.00 -> 25.6 mm
- net Net-(R18-Pad2): track 0.00 -> 17.7 mm
- net HUB75_R0: track 0.00 -> 17.4 mm
- net 3V3: track 0.00 -> 12.3 mm
- net ESP_EN: track 0.00 -> 11.6 mm
- net BTN_A: track 0.00 -> 11.2 mm
- net VUSB_SENSE: track 0.00 -> 8.78 mm
- net BTN_LEFT: track 0.00 -> 7.44 mm
- net BTN_RIGHT: track 0.00 -> 7.10 mm
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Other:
- board size 169 x 56.5 mm -> 161 x 40.1 mm
- net class Default: clearance 0.2 -> 0.3; trace_width 0.25 -> 0.15; via_dia 0.6 -> 0.45; via_drill 0.3 -> 0.2
- net class UART: clearance 0.127 -> 0.15; trace_width 0.127 -> 0.15
- net class USB data: clearance 0.127 -> 0.15; trace_width 0.127 -> 0.15
- rule trace_clearance: 0.2 -> 0.3
- rule trace_min: 0.127 -> 0.15

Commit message: 5mm is hard
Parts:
- moved SW1 162.5 mm to (5.75, -145.0)
- moved SW3 162.5 mm to (2.15, -132.9)
- moved SW5 162.5 mm to (11.2, -132.9)
- moved SW6 162.5 mm to (5.55, -122.0)
- moved U2 42.3 mm to (187.9, -128.3)
- moved U3 42.3 mm to (187.8, -137.8)
- moved U4 42.3 mm to (197.9, -118.8)
- moved U5 42.3 mm to (197.9, -128.3)
- moved U6 42.3 mm to (198.0, -137.8)
- moved SW2 19.8 mm to (77.0, -163.4)
- moved SW4 19.8 mm to (90.5, -163.4)
- moved U10 7.75 mm to (69.8, -138.8)
- moved U1 4.24 mm to (147.8, -121.3), turned to 90 degrees
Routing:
- net Net-(D1-Pad1): track 40.2 -> 174.1 mm, vias 0 -> 2
- net Net-(D130-Pad1): track 40.2 -> 168.2 mm, vias 0 -> 2
- net Net-(D131-Pad1): track 40.2 -> 162.3 mm, vias 0 -> 2
- net Net-(D100-Pad1): track 40.2 -> 156.5 mm, vias 0 -> 2
- net Net-(D101-Pad1): track 40.2 -> 150.6 mm, vias 0 -> 2
- net Net-(D102-Pad1): track 40.2 -> 144.9 mm, vias 0 -> 2
- net Net-(D103-Pad1): track 40.2 -> 139.0 mm, vias 0 -> 2
- net Net-(D104-Pad1): track 40.2 -> 133.0 mm, vias 0 -> 2
- net HUB75_OE: track 0.00 -> 58.0 mm
- net CLK: track 0.00 -> 50.4 mm
- net HUB75_LAT: track 0.00 -> 47.3 mm
- net ESP_TX: track 0.00 -> 32.3 mm, vias 0 -> 2
- net Net-(R24-Pad2): track 0.00 -> 31.8 mm
- net ESP_RX: track 0.00 -> 31.1 mm, vias 0 -> 2
- net USB_DN: track 0.00 -> 13.1 mm
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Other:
- net class Default: clearance 0.3 -> 0.15
- rule trace_clearance: 0.3 -> 0.15

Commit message: Went to 6mm pixel pitch
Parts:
- moved R8 303.8 mm to (29.1, -150.1), turned to 270 degrees
- moved R7 301.7 mm to (29.1, -146.9), turned to 270 degrees
- moved Q1 295.7 mm to (31.7, -146.7)
- moved Q2 294.2 mm to (31.7, -150.3)
- moved Q6 286.3 mm to (149.9, -130.4)
- moved Q5 286.1 mm to (146.0, -130.4)
- moved Q4 285.8 mm to (142.1, -130.5)
- moved R22 285.8 mm to (142.5, -132.6)
- moved SW5 189.1 mm to (200.2, -140.0), turned to 0 degrees
- moved SW6 180.5 mm to (185.2, -140.0)
- moved U9 94.9 mm to (30.6, -110.0), turned to 0 degrees
- moved SW4 75.5 mm to (22.8, -129.9)
- moved U7 67.7 mm to (203.2, -147.9), turned to 90 degrees
- moved SW2 62.8 mm to (30.8, -120.9)
- moved U6 37.1 mm to (163.7, -123.7), turned to 90 degrees
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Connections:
- U7 pad 7: (no net) -> VCC
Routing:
- net Net-(D33-Pad4): track 179.7 -> 379.9 mm, vias 32 -> 64
- net Net-(D100-Pad4): track 179.3 -> 360.3 mm, vias 32 -> 64
- net Net-(D129-Pad4): track 179.7 -> 360.7 mm, vias 32 -> 64
- net Net-(D193-Pad4): track 179.8 -> 352.8 mm, vias 32 -> 62
- net Net-(D161-Pad4): track 182.2 -> 352.0 mm, vias 32 -> 62
- net (no net): track 0.00 -> 158.1 mm, vias 0 -> 32
- net HUB75_OE: track 58.0 -> 0.00 mm
- net BTN_LEFT: track 7.44 -> 64.7 mm, vias 0 -> 2
- net CLK: track 50.4 -> 0.00 mm
- net HUB75_LAT: track 47.3 -> 0.00 mm
- net BTN_DOWN: track 6.20 -> 52.6 mm, vias 0 -> 2
- net C: track 45.9 -> 0.01 mm
- net Net-(D1-Pad4): track 173.6 -> 218.8 mm, vias 0 -> 4
- net BTN_RIGHT: track 7.10 -> 51.4 mm, vias 0 -> 2
- net SCL: track 43.9 -> 0.00 mm
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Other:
- board size 161 x 40.1 mm -> 391.4 x 293.4 mm
- net class USB +5V: clearance 0.2 -> 0.15; trace_width 0.4 -> 0.15
